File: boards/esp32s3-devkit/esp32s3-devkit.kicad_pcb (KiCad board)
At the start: 4 copper layers, 59.3 x 38 mm, 37 parts, among them J1 Conn_01x17_Pin, J2 Conn_01x17_Pin, J3 USB_C_Receptacle_USB2.0_16P, Q1 Q_PMOS_GSD, SW1 ON/OFF, SW2 RESET, SW3 BOOT, U1 TPS630701RNMR, U2 ESP32-S3-WROOM-1, U3 USBLC6-2SC6

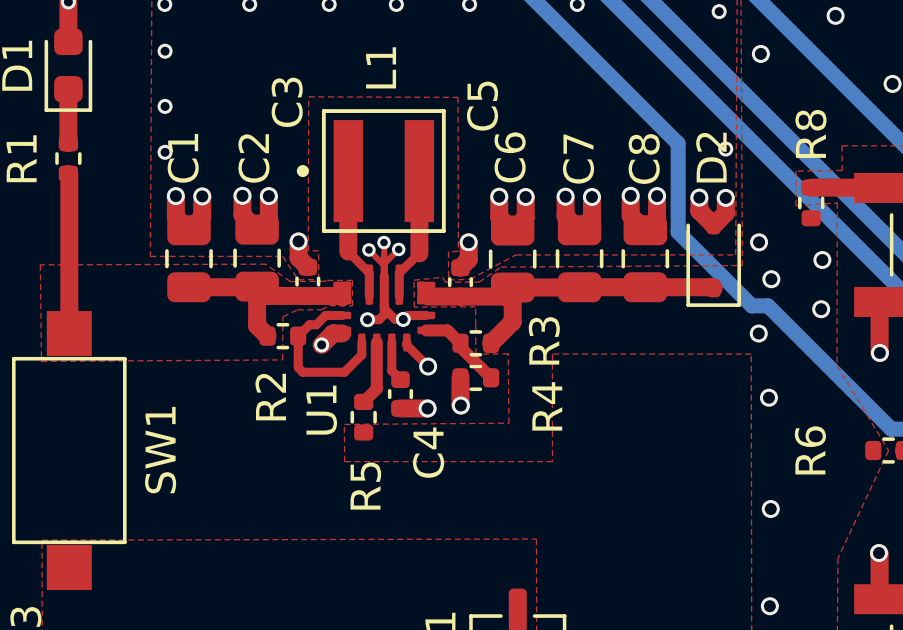
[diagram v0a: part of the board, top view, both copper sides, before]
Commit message: fix(esp32s3-devkit): connect J3 shell pads to GND copper (#97)
Route GND to the USB-C mounting pads so DRC reports zero unconnected items
without relying on zone refill, matching what the update-readmes workflow checks.
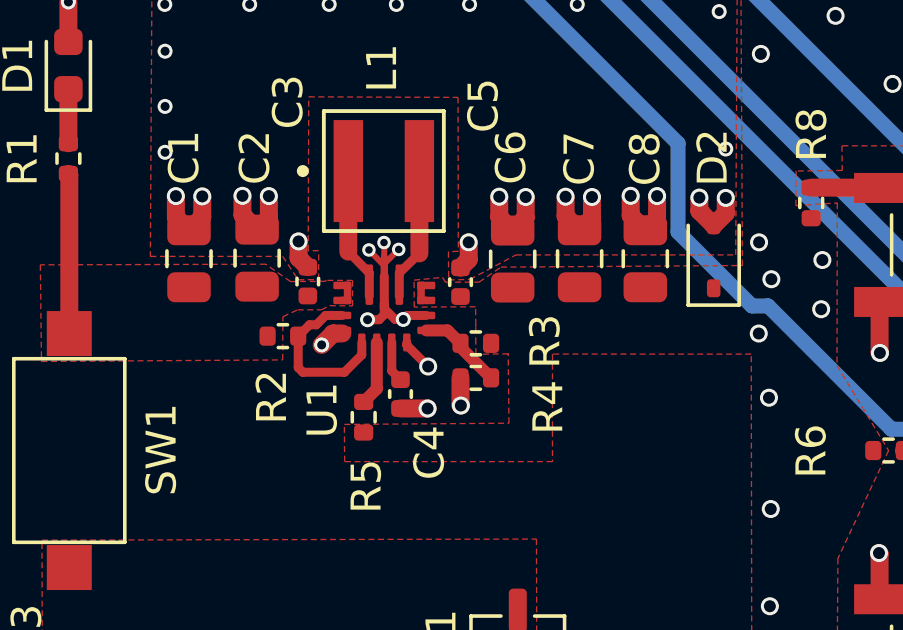
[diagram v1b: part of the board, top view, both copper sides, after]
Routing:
- net /3v3: track 13.2 -> 1.37 mm
- net /2-16v: track 12.4 -> 5.33 mm
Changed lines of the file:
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@@
 		(fp_line
 			(start -9.2 -6.2)
-			(end -9.2 -6.52)
+			(end 9.2 -6.2)
 			(stroke
 				(width 0.12)
@@
 		(fp_line
 			(start -9.2 -6.2)
-			(end 9.2 -6.2)
+			(end -9.2 -6.52)
 			(stroke
 				(width 0.12)
@@
 	)
 	(segment
-		(start 123.1275 96.0875)
-		(end 123.1275 95.4175)
-		(width 0.2)
-		(layer "F.Cu")
-		(net "GND")
-	)
-	(segment
-		(start 123.1275 95.4175)
-		(end 123.1275 94.9775)
-		(width 0.2)
-		(layer "F.Cu")
-		(net "GND")
-	)
-	(segment
-		(start 123.1275 94.9775)
-		(end 123.1175 94.9675)
-		(width 0.2)
-		(layer "F.Cu")
-		(net "GND")
-	)
-	(segment
-		(start 123.1275 95.742)
-		(end 123.1275 96.0875)
-		(width 0.2)
-		(layer "F.Cu")
-		(net "GND")
-	)
-	(segment
-		(start 122.6152 95.2148)
-		(end 123.1275 95.742)
-		(width 0.2)
-		(layer "F.Cu")
-		(net "GND")
-	)
-	(segment
-		(start 123.6075 95.1975)
-		(end 123.1275 95.6775)
-		(width 0.2)
-		(layer "F.Cu")
-		(net "GND")
-	)
-	(segment
-		(start 123.1275 95.6775)
-		(end 123.1275 96.0875)
-		(width 0.2)
-		(layer "F.Cu")
-		(net "GND")
-	)
-	(segment
 		(start 145.9375 105.3575)
 		(end 145.9575 105.3375)
@@
 	)
 	(segment
+		(start 123.1275 95.4175)
+		(end 123.1275 94.9775)
+		(width 0.2)
+		(layer "F.Cu")
+		(net "GND")
+	)
+	(segment
 		(start 125.6375 111.1375)
 		(end 125.6275 111.1275)
@@
 	)
 	(segment
+		(start 123.6075 95.1975)
+		(end 123.1275 95.6775)
+		(width 0.2)
+		(layer "F.Cu")
+		(net "GND")
+	)
+	(segment
 		(start 123.1275 97.0075)
 		(end 123.1275 97.3675)
@@
 	)
 	(segment
+		(start 123.1275 96.0875)
+		(end 123.1275 95.4175)
+		(width 0.2)
+		(layer "F.Cu")
+		(net "GND")
+	)
+	(segment
+		(start 122.6152 95.2148)
+		(end 123.1275 95.742)
+		(width 0.2)
+		(layer "F.Cu")
+		(net "GND")
+	)
+	(segment
 		(start 119.28 94.145)
 		(end 118.8875 94.5375)
@@
 	)
 	(segment
+		(start 123.1275 94.9775)
+		(end 123.1175 94.9675)
+		(width 0.2)
+		(layer "F.Cu")
+		(net "GND")
+	)
+	(segment
 		(start 122.955 97.54)
 		(end 122.57 97.54)
@@
 	)
 	(segment
+		(start 123.1275 95.742)
+		(end 123.1275 96.0875)
+		(width 0.2)
+		(layer "F.Cu")
+		(net "GND")
+	)
+	(segment
 		(start 168.2575 91.5175)
 		(end 168.2675 91.5075)
@@
 	)
 	(segment
+		(start 123.1275 95.6775)
+		(end 123.1275 96.0875)
+		(width 0.2)
+		(layer "F.Cu")
+		(net "GND")
+	)
+	(segment
 		(start 118.6225 111.0175)
 		(end 120.12 109.52)
@@
 	)
 	(segment
-		(start 120.5775 96.7475)
-		(end 121.6775 96.7475)
-		(width 0.6)
-		(layer "F.Cu")
-		(net "/2-16v")
-	)
-	(segment
-		(start 118.8875 96.4375)
-		(end 119.1975 96.7475)
-		(width 0.6)
-		(layer "F.Cu")
-		(net "/2-16v")
-	)
-	(segment
-		(start 118.8675 96.4575)
-		(end 118.8875 96.4375)
-		(width 0.6)
-		(layer "F.Cu")
-		(net "/2-16v")
-	)
-	(segment
-		(start 121.6775 96.7475)
-		(end 121.7275 96.7975)
-		(width 0.6)
-		(layer "F.Cu")
-		(net "/2-16v")
-	)
-	(segment
 		(start 112.627499 92.707499)
 		(end 112.5975 92.6775)
@@
 	)
 	(segment
-		(start 116.6175 96.4575)
-		(end 118.8675 96.4575)
-		(width 0.6)
-		(layer "F.Cu")
-		(net "/2-16v")
-	)
-	(segment
 		(start 112.627499 98)
 		(end 112.627499 92.707499)
@@
 	)
 	(segment
-		(start 119.1975 96.7475)
-		(end 120.5775 96.7475)
-		(width 0.6)
-		(layer "F.Cu")
-		(net "/2-16v")
-	)
-	(segment
-		(start 118.8875 96.4375)
-		(end 118.8875 97.7375)
-		(width 0.6)
-		(layer "F.Cu")
-		(net "/2-16v")
-	)
-	(segment
-		(start 118.8875 97.7375)
-		(end 119.2375 98.0875)
-		(width 0.6)
-		(layer "F.Cu")
-		(net "/2-16v")
-	)
-	(segment
 		(start 121.173972 97.3975)
 		(end 121.7275 97.3975)
@@
 	)
 	(segment
-		(start 127.4075 96.4675)
-		(end 129.6275 96.4675)
-		(width 0.6)
-		(layer "F.Cu")
-		(net "/3v3")
-	)
-	(segment
-		(start 127.4075 97.6075)
-		(end 126.6875 98.3275)
-		(width 0.6)
-		(layer "F.Cu")
-		(net "/3v3")
-	)
-	(segment
 		(start 165.7 88.49)
 		(end 165.7 89.84)
@@
 	)
 	(segment
-		(start 125.6675 96.7675)
-		(end 124.5825 96.7675)
-		(width 0.6)
-		(layer "F.Cu")
-		(net "/3v3")
-	)
-	(segment
-		(start 134.073 96.4575)
-		(end 134.1075 96.492)
-		(width 0.6)
-		(layer "F.Cu")
-		(net "/3v3")
-	)
-	(segment
-		(start 127.1075 96.7675)
-		(end 127.4075 96.4675)
-		(width 0.6)
-		(layer "F.Cu")
-		(net "/3v3")
-	)
-	(segment
-		(start 127.4075 96.4675)
-		(end 127.4075 97.6075)
-		(width 0.6)
-		(layer "F.Cu")
-		(net "/3v3")
-	)
-	(segment
-		(start 125.6675 96.7675)
-		(end 127.1075 96.7675)
-		(width 0.6)
-		(layer "F.Cu")
-		(net "/3v3")
-	)
-	(segment
-		(start 129.6275 96.4675)
-		(end 129.6375 96.4575)
-		(width 0.6)
-		(layer "F.Cu")
-		(net "/3v3")
-	)
-	(segment
-		(start 131.8275 96.4575)
-		(end 134.073 96.4575)
-		(width 0.6)
-		(layer "F.Cu")
-		(net "/3v3")
-	)
-	(segment
-		(start 129.6375 96.4575)
-		(end 131.8275 96.4575)
-		(width 0.6)
-		(layer "F.Cu")
-		(net "/3v3")
-	)
-	(segment
 		(start 165.7 89.84)
 		(end 165.7175 89.8575)
@@
 	)
 	(segment
-		(start 121.9275 92.5845)
-		(end 121.9275 95.2695)
+		(start 123.6275 96.7595)
+		(end 123.6275 95.9845)
+		(width 0.3)
+		(layer "F.Cu")
+		(net "Net-(U1-L2)")
+	)
+	(segment
+		(start 124.2975 92.5845)
+		(end 124.2975 95.3295)
 		(width 0.6)
 		(layer "F.Cu")
-		(net "Net-(U1-L1)")
+		(net "Net-(U1-L2)")
 	)
 	(segment
-		(start 121.9275 95.2695)
-		(end 122.6275 95.9845)
+		(start 124.2975 95.3295)
+		(end 123.6275 95.9845)
 		(width 0.3)
 		(layer "F.Cu")
-		(net "Net-(U1-L1)")
+		(net "Net-(U1-L2)")
 	)
 	(segment
@@
 	)
 	(segment
-		(start 124.2975 92.5845)
-		(end 124.2975 95.3295)
+		(start 121.9275 92.5845)
+		(end 121.9275 95.2695)
 		(width 0.6)
 		(layer "F.Cu")
-		(net "Net-(U1-L2)")
-	)
-	(segment
-		(start 124.2975 95.3295)
-		(end 123.6275 95.9845)
-		(width 0.3)
-		(layer "F.Cu")
-		(net "Net-(U1-L2)")
+		(net "Net-(U1-L1)")
 	)
 	(segment
-		(start 123.6275 96.7595)
-		(end 123.6275 95.9845)
+		(start 121.9275 95.2695)
+		(end 122.6275 95.9845)
 		(width 0.3)
 		(layer "F.Cu")
-		(net "Net-(U1-L2)")
+		(net "Net-(U1-L1)")
 	)
 	(segment
